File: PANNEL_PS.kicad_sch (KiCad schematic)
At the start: 22 parts, among them IC28 INA226AIDGSR, IC29 TPS25940ARVCR

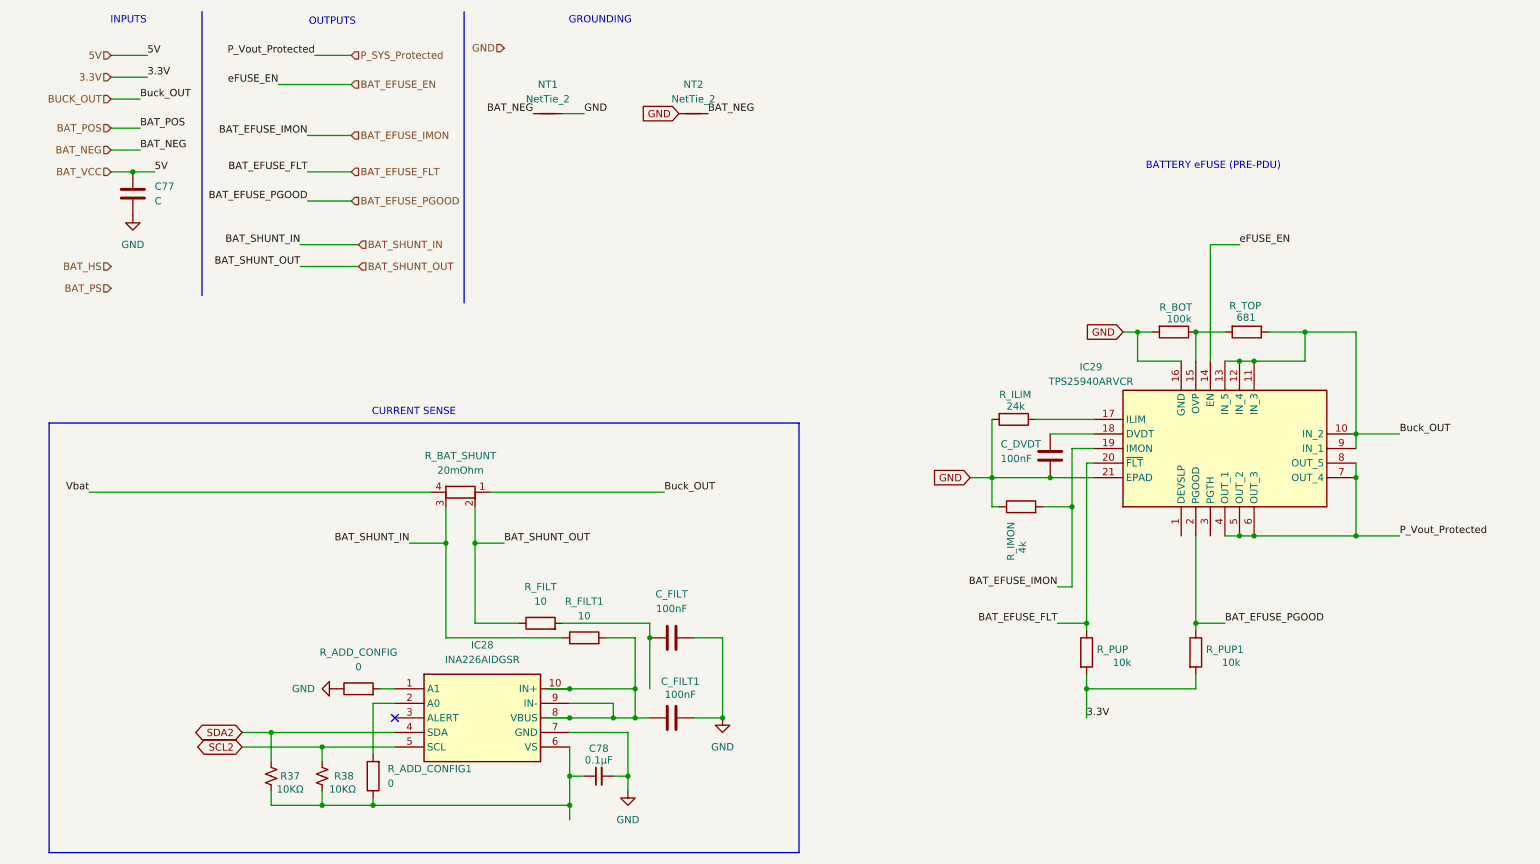
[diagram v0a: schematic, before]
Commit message: Created a page for PANNEL efuse, modifiel all to local labels, functionally finished
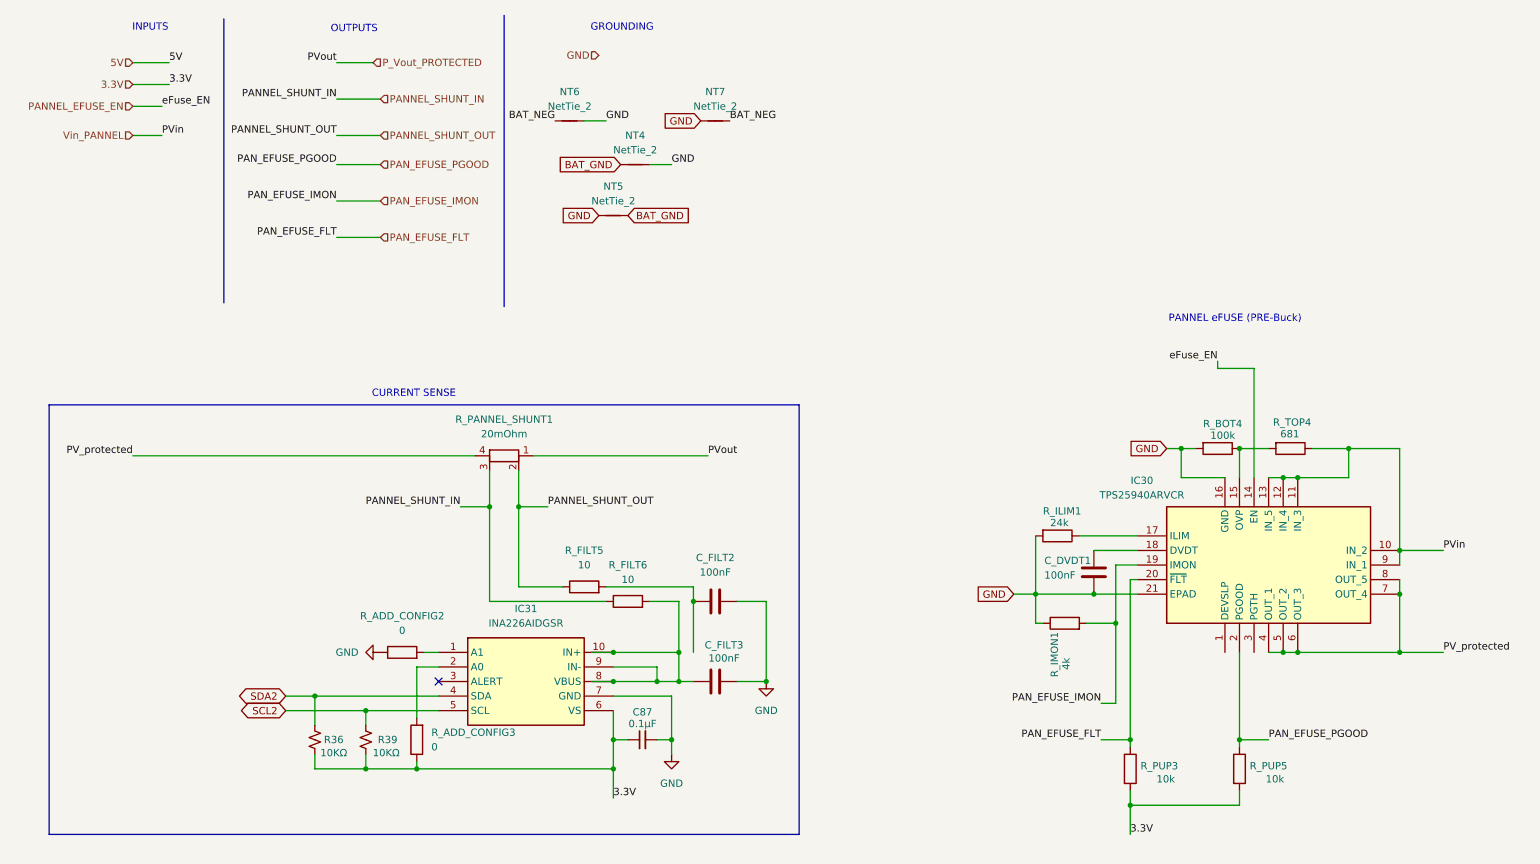
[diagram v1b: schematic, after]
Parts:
- removed C77: C, symbol Device:C
- removed C78: 0.1μF, C0603, symbol Device:C_Small
- removed C_DVDT, C_FILT, C_FILT1: 100nF, symbol Device:C
- removed IC28: INA226AIDGSR, SOP50P490X110-10N, symbol PDU_Library:INA226AIDGSR
- removed IC29: TPS25940ARVCR, PULSE_Library:QFN50P300X400X80-21N, symbol PULSE_Library:TPS25940ARVCR
- removed NT1, NT2: NetTie_2, symbol Device:NetTie_2
- removed R37, R38: 10KΩ, RESC1608X55N, symbol Device:R_Small_US
- removed R_ADD_CONFIG, R_ADD_CONFIG1: 0, symbol Device:R
- removed R_BAT_SHUNT: 20mOhm, symbol Device:R_Shunt
- removed R_BOT: 100k, symbol Device:R
- removed R_FILT, R_FILT1: 10, symbol Device:R
- removed R_ILIM: 24k, symbol Device:R
- removed R_IMON: 4k, symbol Device:R
- removed R_PUP, R_PUP1: 10k, symbol Device:R
- removed R_TOP: 681, symbol Device:R
- added C87: 0.1μF, C0603, symbol Device:C_Small
- added C_DVDT1, C_FILT2, C_FILT3: 100nF, symbol Device:C
- added IC30: TPS25940ARVCR, PULSE_Library:QFN50P300X400X80-21N, symbol PULSE_Library:TPS25940ARVCR
- added IC31: INA226AIDGSR, SOP50P490X110-10N, symbol PDU_Library:INA226AIDGSR
- added NT4, NT5, NT6, NT7: NetTie_2, symbol Device:NetTie_2
- added R36, R39: 10KΩ, RESC1608X55N, symbol Device:R_Small_US
- added R_ADD_CONFIG2, R_ADD_CONFIG3: 0, symbol Device:R
- added R_BOT4: 100k, symbol Device:R
- added R_FILT5, R_FILT6: 10, symbol Device:R
- added R_ILIM1: 24k, symbol Device:R
- added R_IMON1: 4k, symbol Device:R
- added R_PANNEL_SHUNT1: 20mOhm, symbol Device:R_Shunt
- added R_PUP3, R_PUP5: 10k, symbol Device:R
- added R_TOP4: 681, symbol Device:R
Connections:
- net 3.3V: now also C87.1, IC31.6 (VS), R36.2, R39.2, R_ADD_CONFIG3.1, R_PUP3.2, R_PUP5.2
- net BAT_NEG: now also NT6.1, NT7.2
- net GND: now also C87.2, C_DVDT1.1, C_FILT2.2, C_FILT3.2, IC30.16 (GND), IC30.21 (EPAD), IC31.7 (GND), NT4.2, NT5.1, NT6.2, NT7.1, R_ADD_CONFIG2.1, R_BOT4.2, R_ILIM1.2, R_IMON1.1
- net SCL2: now also IC31.5 (SCL), R39.1
- net SDA2: now also IC31.4 (SDA), R36.1
- new net: IC31.1 (A1), R_ADD_CONFIG2.2
- new net: C_FILT3.1, IC31.10 (IN+), IC31.8 (VBUS), IC31.9 (IN-), R_FILT6.2
- new net: IC31.2 (A0), R_ADD_CONFIG3.2
- new net: C_FILT2.1, R_FILT5.2
- new net: IC30.15 (OVP), R_BOT4.1, R_TOP4.2
- new net: C_DVDT1.2, IC30.18 (DVDT)
- new net: IC30.17 (ILIM), R_ILIM1.1
- new net BAT_GND: NT4.1, NT5.2
- new net PANNEL_EFUSE_EN: IC30.14 (EN)
- new net PANNEL_SHUNT_IN: R_FILT6.1, R_PANNEL_SHUNT1.3
- new net PANNEL_SHUNT_OUT: R_FILT5.1, R_PANNEL_SHUNT1.2
- new net PAN_EFUSE_FLT: IC30.20 (~{FLT}), R_PUP3.1
- new net PAN_EFUSE_IMON: IC30.19 (IMON), R_IMON1.2
- new net PAN_EFUSE_PGOOD: IC30.2 (PGOOD), R_PUP5.1
- new net PV_protected: IC30.4 (OUT_1), IC30.5 (OUT_2), IC30.6 (OUT_3), IC30.7 (OUT_4), IC30.8 (OUT_5), R_PANNEL_SHUNT1.4
- new net P_Vout_PROTECTED: R_PANNEL_SHUNT1.1
- new net Vin_PANNEL: IC30.10 (IN_2), IC30.11 (IN_3), IC30.12 (IN_4), IC30.13 (IN_5), IC30.9 (IN_1), R_TOP4.1
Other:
- note added: "PANNEL eFUSE (PRE-Buck)"
- note removed: "BATTERY eFUSE (PRE-PDU)"

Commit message: Some edits
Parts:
- removed NT4, NT5, NT6, NT7: NetTie_2, symbol Device:NetTie_2
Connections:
- net 3.3V: no longer R_ADD_CONFIG3.1
- net SCL2: now also R_ADD_CONFIG3.1
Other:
- moved on the sheet: R36, R39, R_ADD_CONFIG3

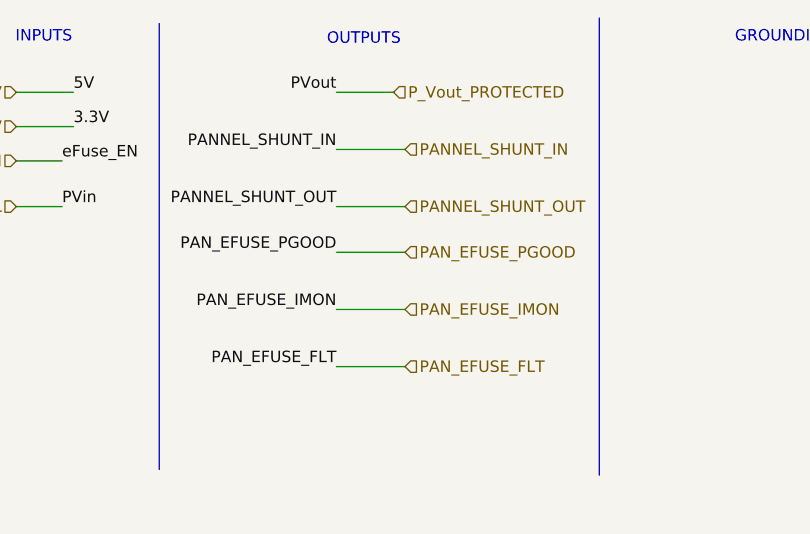
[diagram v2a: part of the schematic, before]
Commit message: Modification of ROOT sheet blocks
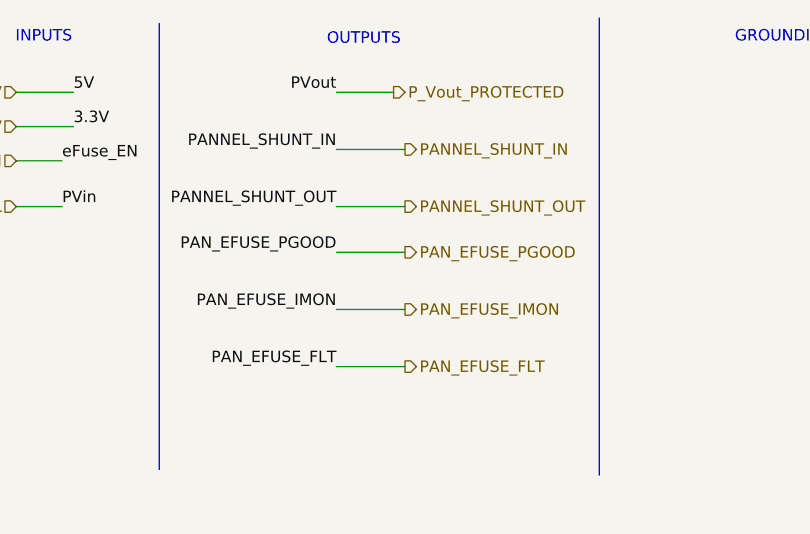
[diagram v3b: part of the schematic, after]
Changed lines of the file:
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@@
 	)
 	(hierarchical_label "PAN_EFUSE_FLT"
-		(shape input)
+		(shape output)
 		(at 76.2 53.34 0)
 		(effects
@@
 	)
 	(hierarchical_label "P_Vout_PROTECTED"
-		(shape input)
+		(shape output)
 		(at 74.93 22.86 0)
 		(effects
@@
 	)
 	(hierarchical_label "PAN_EFUSE_IMON"
-		(shape input)
+		(shape output)
 		(at 76.2 46.99 0)
 		(effects
@@
 	)
 	(hierarchical_label "PAN_EFUSE_PGOOD"
-		(shape input)
+		(shape output)
 		(at 76.2 40.64 0)
 		(effects
@@
 	)
 	(hierarchical_label "PANNEL_SHUNT_IN"
-		(shape input)
+		(shape output)
 		(at 76.2 29.21 0)
 		(effects
@@
 	)
 	(hierarchical_label "PANNEL_SHUNT_OUT"
-		(shape input)
+		(shape output)
 		(at 76.2 35.56 0)
 		(effects

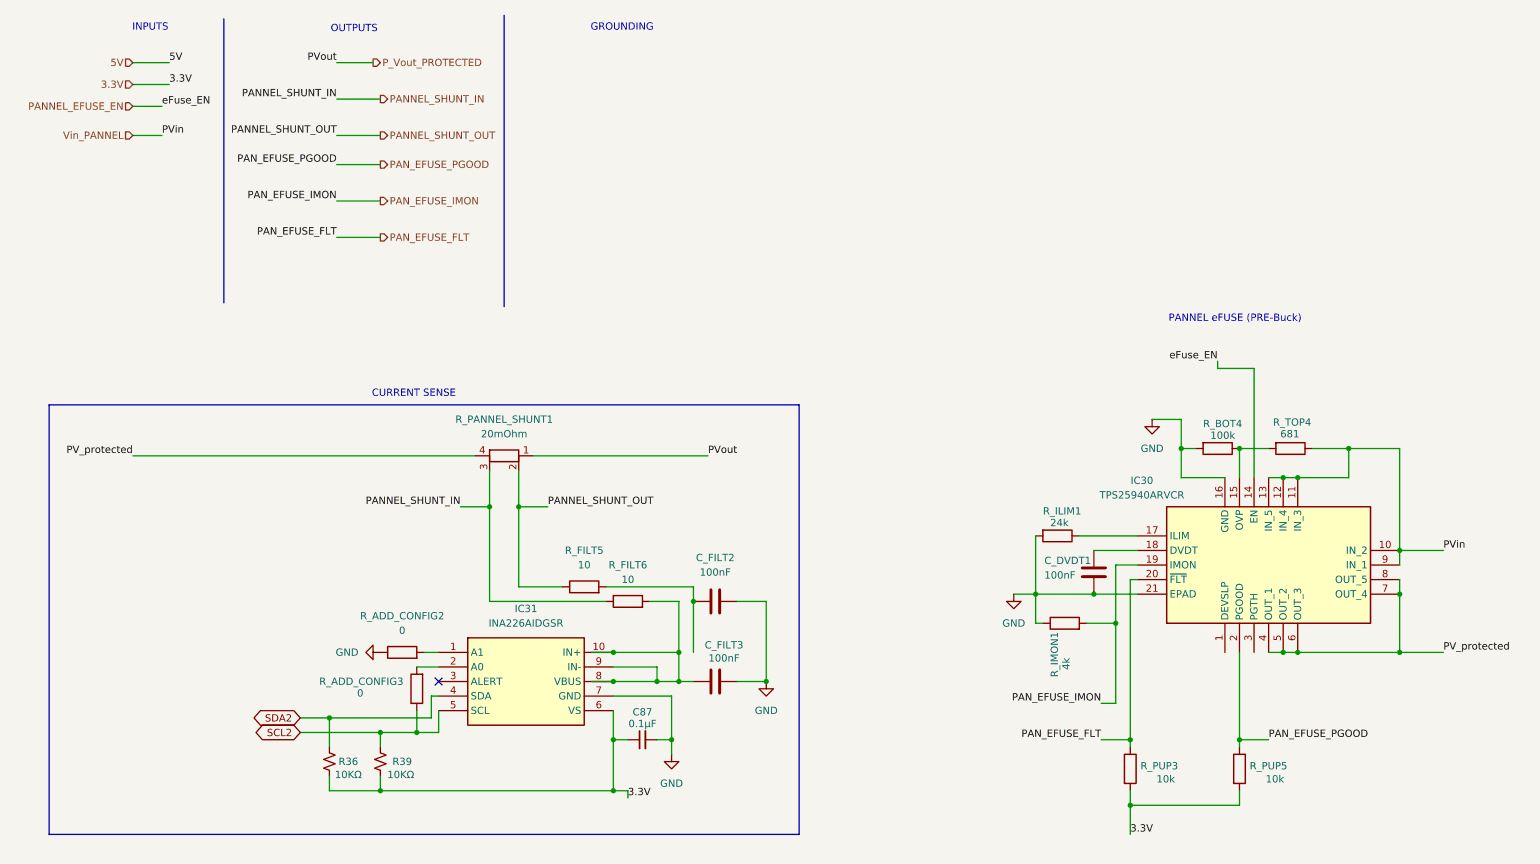
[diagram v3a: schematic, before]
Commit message: Adjusting footprints of components
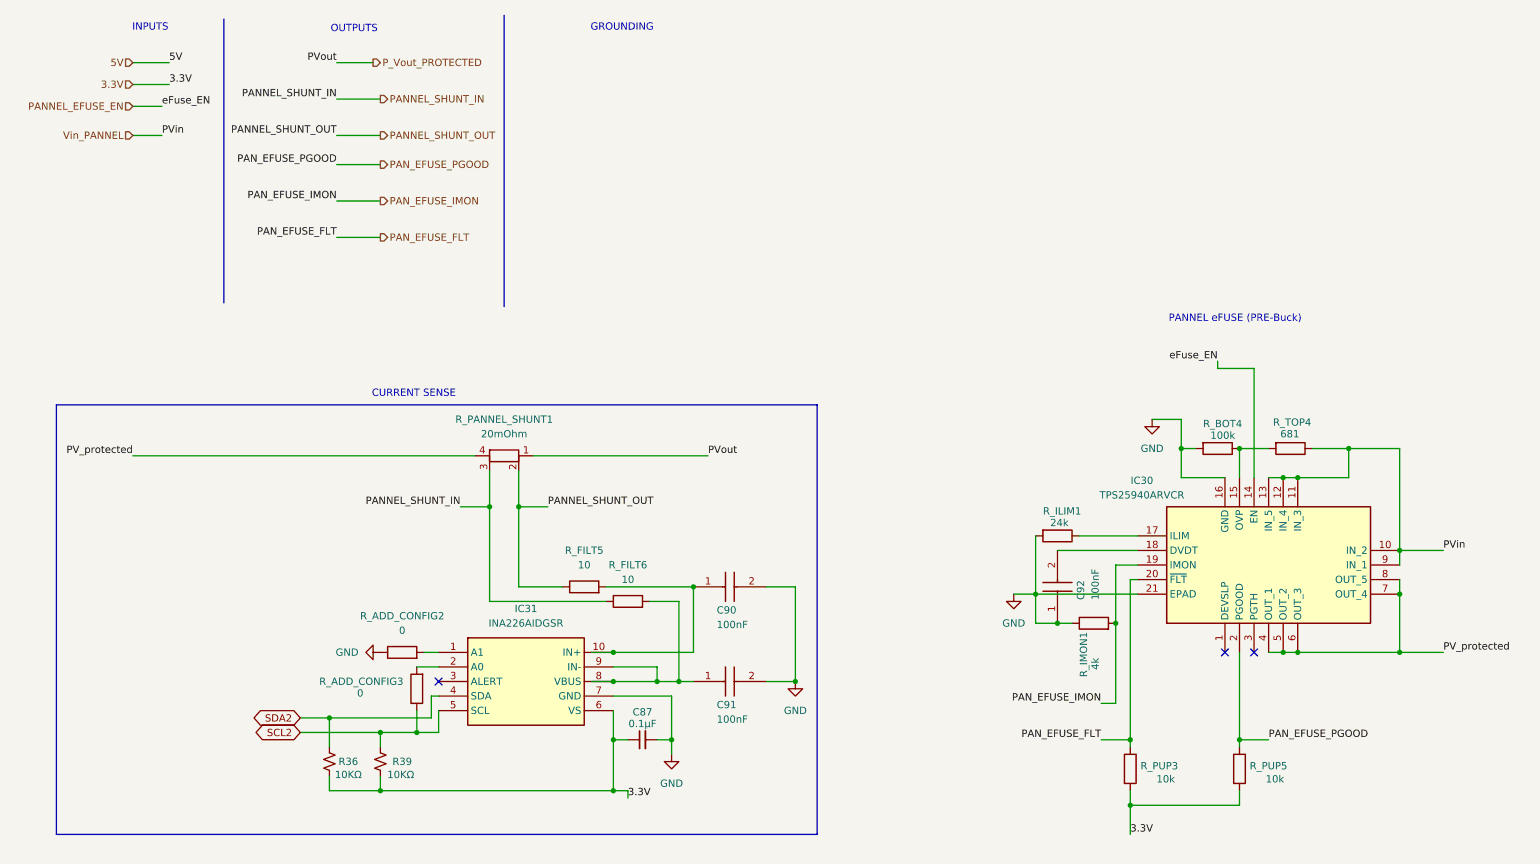
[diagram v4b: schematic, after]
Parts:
- removed C_DVDT1, C_FILT2, C_FILT3: 100nF, symbol Device:C
- added C90, C91, C92: 100nF, C0603_Commercial, symbol PULSE_Library:C0603X6S0J104M030BC
- C87: footprint C0603 -> PULSE_Library:C0603
- IC31: footprint SOP50P490X110-10N -> PULSE_Library:SOP50P490X110-10N
- R36, R39: footprint RESC1608X55N -> PULSE_Library:RESC1608X55N
- R_ADD_CONFIG2, R_ADD_CONFIG3, R_BOT4, R_FILT5, R_FILT6, R_ILIM1, R_IMON1, R_PUP3, R_PUP5, R_TOP4: footprint (none) -> Resistor_SMD:R_0603_1608Metric
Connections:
- net GND: now also C90.2, C91.2, C92.1
- net at IC31.8 (VBUS), IC31.9 (IN-), R_FILT6.2: now also C91.1; no longer IC31.10 (IN+)
- net at R_FILT5.2: now also IC31.10 (IN+), C90.1
- net at IC30.18 (DVDT): now also C92.2
- no-connect marks 1 -> 3
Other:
- moved on the sheet: R_IMON1

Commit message: Big final PCU PCB design
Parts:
- added R_BYPASS15: 0, Resistor_SMD:R_0603_1608Metric, symbol Device:R
- added TP28: P_Vout_Protected, TestPoint:TestPoint_Pad_D2.0mm, symbol Connector:TestPoint_Probe
- added TP29: PVin, TestPoint:TestPoint_Pad_D2.0mm, symbol Connector:TestPoint_Probe
- added TP30: eFuse_EN, TestPoint:TestPoint_Pad_D2.0mm, symbol Connector:TestPoint_Probe
- added TP31: eFuse_OVP, TestPoint:TestPoint_Pad_D2.0mm, symbol Connector:TestPoint_Probe
- C90, C91, C92: footprint C0603_Commercial -> Capacitor_SMD:C_0603_1608Metric
- R_PANNEL_SHUNT1: footprint (none) -> Resistor_SMD:R_Shunt_Vishay_WSKW0612
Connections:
- net PANNEL_EFUSE_EN: now also TP30.1
- net PV_protected: now also R_BYPASS15.2, TP28.1
- net Vin_PANNEL: now also R_BYPASS15.1, TP29.1
- net at IC30.15 (OVP), R_BOT4.1, R_TOP4.2: now also TP31.1
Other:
- moved on the sheet: C87, C90, C91, C92, IC30, IC31, R36, R39, R_ADD_CONFIG2, R_ADD_CONFIG3, R_BOT4, R_FILT5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
